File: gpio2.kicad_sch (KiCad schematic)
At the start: 2 parts, among them U27 RK3576

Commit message: Add files via upload
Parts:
- renumbered C329 to C99, U27 to U2
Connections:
- net PCIe_CLKREQ: no longer U2.1A17 (VI_CIF_D11)
- net PCIe_RESET: no longer U2.1A18 (VI_CIF_D12)
- net TYPEC_PWR-IN_SEL1: now reaches U2.1C18 (VI_CIF_D8)
- net TYPEC_PWR-IN_SEL2: now reaches U2.A21 (VI_CIF_D7)
- new net PCIE0_CLKREQn_M0: U2.1A17 (VI_CIF_D11)
- new net PCIE0_RESETn: U2.1A18 (VI_CIF_D12)
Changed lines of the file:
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@@
 		)
 	)
-	(label "PCIe_RESET"
+	(label "PCIE0_RESETn"
 		(at 147.32 53.34 180)
 		(effects
@@
 		)
 	)
+	(label "TYPEC_PWR-IN_SEL1"
+		(at 160.02 63.5 180)
+		(effects
+			(font
+				(size 1.016 1.016)
+			)
+			(justify right bottom)
+		)
+	)
 	(label "PCIe_WAKE"
 		(at 162.56 38.1 0)
@@
 		)
 	)
-	(label "PCIe_CLKREQ"
+	(label "PCIE0_CLKREQn_M0"
 		(at 147.32 55.88 180)
+		(effects
+			(font
+				(size 1.016 1.016)
+			)
+			(justify right bottom)
+		)
+	)
+	(label "TYPEC_PWR-IN_SEL2"
+		(at 160.02 66.04 180)
 		(effects
 			(font
@@
 		)
 	)
-	(hierarchical_label "PCIe_CTRL"
+	(hierarchical_label "PCIE0_CTRL"
 		(shape bidirectional)
 		(at 184.15 31.75 0)
+		(fields_autoplaced yes)
 		(effects
 			(font
@@
 			)
 			(justify left)
+		)
+		(property "Netclass" "PCIE0_CTRL"
+			(at 184.15 33.02 0)
+			(hide yes)
+			(show_name no)
+			(do_not_autoplace no)
+			(effects
+				(font
+					(size 1.27 1.27)
+					(italic yes)
+				)
+				(justify left)
+			)
 		)
 	)
@@
 			)
 			(justify left)
+		)
+	)
+	(rule_area
+		(exclude_from_sim no)
+		(in_bom yes)
+		(on_board yes)
+		(dnp no)
+		(polyline
+			(pts
+				(xy 129.54 67.31) (xy 130.81 66.04) (xy 147.32 66.04) (xy 148.59 67.31) (xy 148.59 82.55) (xy 147.32 83.82)
+				(xy 130.81 83.82) (xy 129.54 82.55)
+			)
+			(stroke
+				(width 0)
+				(type dash)
+			)
+			(fill
+				(type none)
+			)
 		)
 	)
@@
 		(in_pos_files yes)
 		(dnp no)
-		(property "Reference" "U27"
-			(at 101.092 27.94 0)
+		(property "Reference" "U2"
+			(at 101.092 35.306 0)
 			(show_name no)
 			(do_not_autoplace no)
@@
 		)
 		(property "Value" "RK3576"
-			(at 101.092 30.48 0)
+			(at 101.092 37.846 0)
 			(show_name no)
 			(do_not_autoplace no)
@@
 		(property "Manf" "Rockchip"
 			(at 101.092 33.02 0)
+			(hide yes)
 			(show_name no)
 			(do_not_autoplace no)
@@
 		(property "MPN" "RK3576"
 			(at 101.092 35.56 0)
+			(hide yes)
 			(show_name no)
 			(do_not_autoplace no)
@@
 		(property "Package" "FCCSP698L"
 			(at 101.092 38.1 0)
+			(hide yes)
+			(show_name no)
+			(do_not_autoplace no)
+			(effects
+				(font
+					(size 1.27 1.27)
+				)
+			)
+		)
+		(property "Dielectric" ""
+			(at 101.6 68.58 0)
+			(hide yes)
+			(show_name no)
+			(do_not_autoplace no)
+			(effects
+				(font
+					(size 1.27 1.27)
+				)
+			)
+		)
+		(property "Voltage" ""
+			(at 101.6 68.58 0)
+			(hide yes)
+			(show_name no)
+			(do_not_autoplace no)
+			(effects
+				(font
+					(size 1.27 1.27)
+				)
+			)
+		)
+		(property "KLC_S3.3" ""
+			(at 101.6 68.58 0)
+			(hide yes)
+			(show_name no)
+			(do_not_autoplace no)
+			(effects
+				(font
+					(size 1.27 1.27)
+				)
+			)
+		)
+		(property "KLC_S4.1" ""
+			(at 101.6 68.58 0)
+			(hide yes)
+			(show_name no)
+			(do_not_autoplace no)
+			(effects
+				(font
+					(size 1.27 1.27)
+				)
+			)
+		)
+		(property "KLC_S5.1" ""
+			(at 101.6 68.58 0)
+			(hide yes)
 			(show_name no)
 			(do_not_autoplace no)
@@
 			(project "RK3576 SBC"
 				(path "/b79dbff4-0cad-4ff7-bec2-7c0e4f8b14d3/34f9b0cb-aeae-42b4-a2af-a0a79afcf392/90f1d3d6-11a1-4fbf-aa1e-f6ffe7a54522"
-					(reference "U27")
+					(reference "U2")
 					(unit 3)
 				)
@@
 		(in_pos_files yes)
 		(dnp no)
-		(property "Reference" "#PWR0425"
+		(property "Reference" "#PWR0136"
 			(at 60.96 48.26 0)
 			(hide yes)
@@
 			(project "RK3576 SBC"
 				(path "/b79dbff4-0cad-4ff7-bec2-7c0e4f8b14d3/34f9b0cb-aeae-42b4-a2af-a0a79afcf392/90f1d3d6-11a1-4fbf-aa1e-f6ffe7a54522"
-					(reference "#PWR0425")
+					(reference "#PWR0136")
 					(unit 1)
 				)
@@
 		(dnp no)
 		(fields_autoplaced yes)
-		(property "Reference" "C329"
+		(property "Reference" "C99"
 			(at 63.5 45.7262 0)
 			(show_name no)
@@
 		)
 		(property "Description" "Unpolarized capacitor, small symbol"
+			(at 60.96 46.99 0)
+			(hide yes)
+			(show_name no)
+			(do_not_autoplace no)
+			(effects
+				(font
+					(size 1.27 1.27)
+				)
+			)
+		)
+		(property "Dielectric" ""
+			(at 60.96 46.99 0)
+			(hide yes)
+			(show_name no)
+			(do_not_autoplace no)
+			(effects
+				(font
+					(size 1.27 1.27)
+				)
+			)
+		)
+		(property "Voltage" ""
+			(at 60.96 46.99 0)
+			(hide yes)
+			(show_name no)
+			(do_not_autoplace no)
+			(effects
+				(font
+					(size 1.27 1.27)
+				)
+			)
+		)
+		(property "KLC_S3.3" ""
+			(at 60.96 46.99 0)
+			(hide yes)
+			(show_name no)
+			(do_not_autoplace no)
+			(effects
+				(font
+					(size 1.27 1.27)
+				)
+			)
+		)
+		(property "KLC_S4.1" ""
+			(at 60.96 46.99 0)
+			(hide yes)
+			(show_name no)
+			(do_not_autoplace no)
+			(effects
+				(font
+					(size 1.27 1.27)
+				)
+			)
+		)
+		(property "KLC_S5.1" ""
 			(at 60.96 46.99 0)
 			(hide yes)
@@
 			(project "RK3576 SBC"
 				(path "/b79dbff4-0cad-4ff7-bec2-7c0e4f8b14d3/34f9b0cb-aeae-42b4-a2af-a0a79afcf392/90f1d3d6-11a1-4fbf-aa1e-f6ffe7a54522"
-					(reference "C329")
+					(reference "C99")
 					(unit 1)
 				)
@@
 		(in_pos_files yes)
 		(dnp no)
-		(property "Reference" "#PWR0426"
+		(property "Reference" "#PWR0137"
 			(at 60.96 55.88 0)
 			(hide yes)
@@
 			(project "RK3576 SBC"
 				(path "/b79dbff4-0cad-4ff7-bec2-7c0e4f8b14d3/34f9b0cb-aeae-42b4-a2af-a0a79afcf392/90f1d3d6-11a1-4fbf-aa1e-f6ffe7a54522"
-					(reference "#PWR0426")
+					(reference "#PWR0137")
 					(unit 1)
 				)

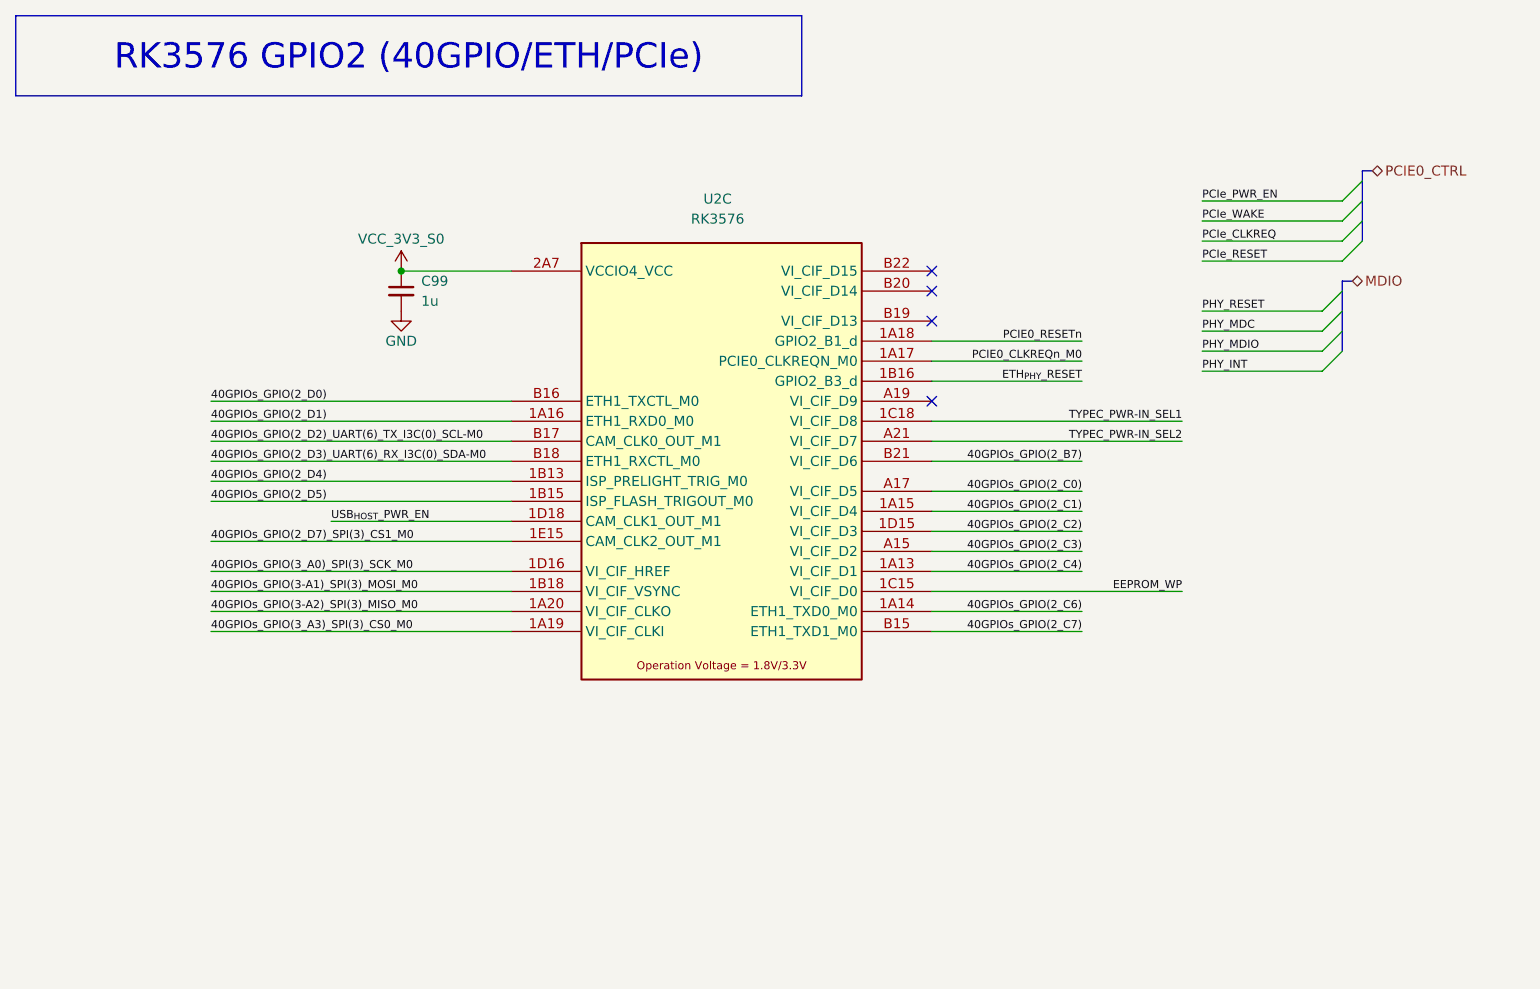
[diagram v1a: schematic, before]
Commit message: SBC Board V0.2
The SBC schematics before footprint and part number check
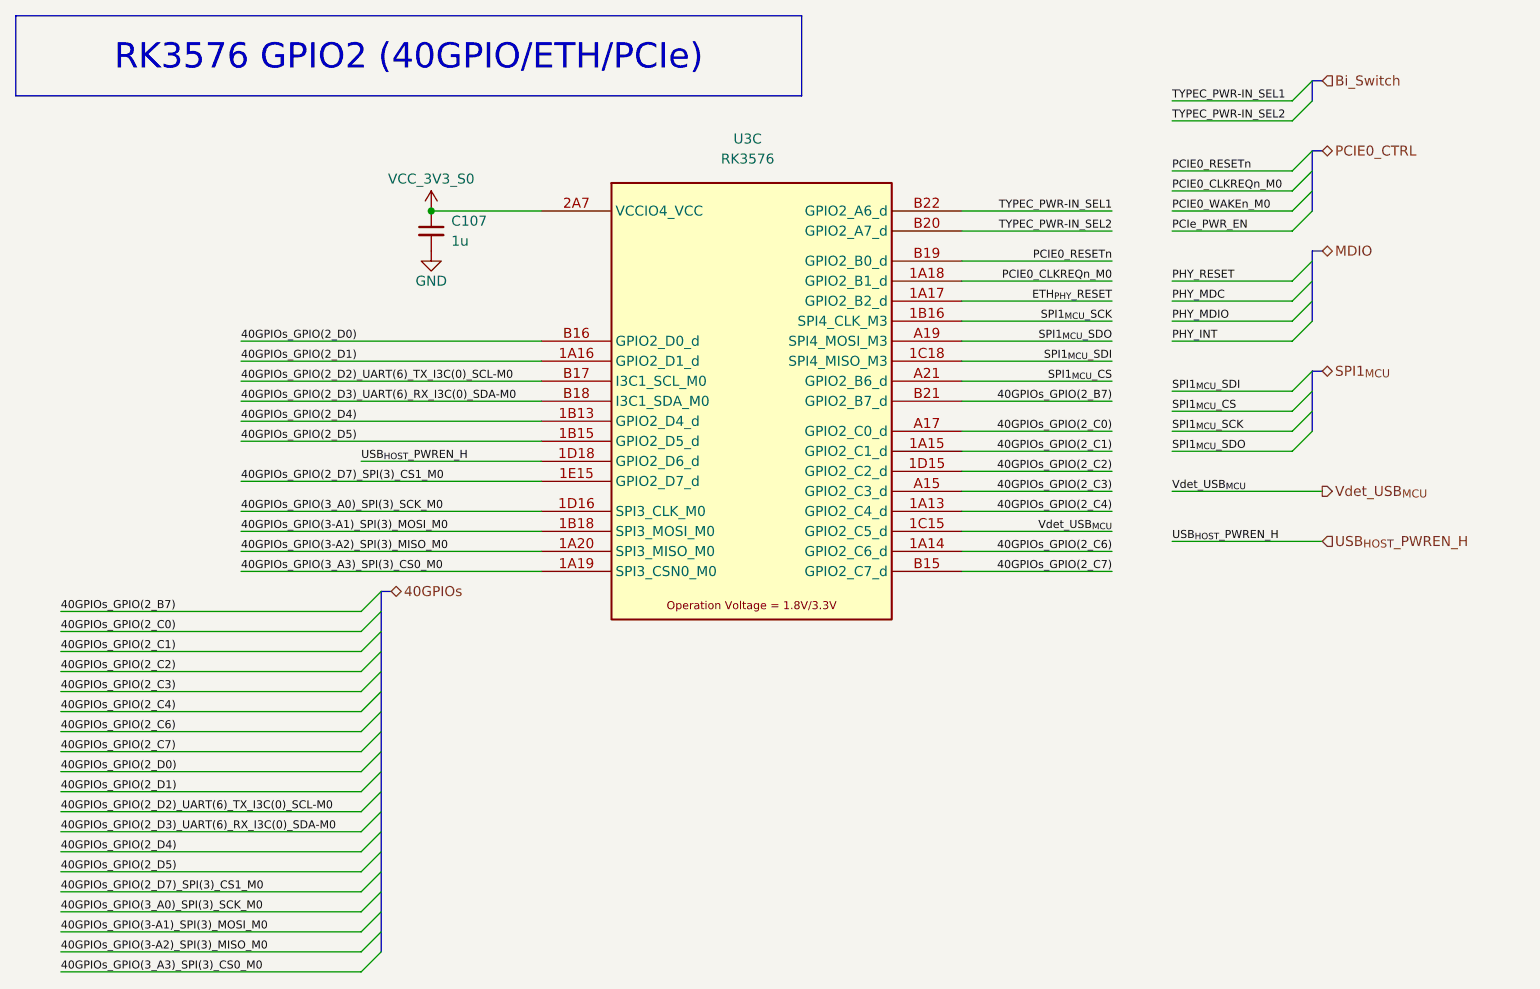
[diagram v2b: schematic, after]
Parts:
- U3: renamed from U2; footprint (none) -> easyeda2kicad:FCCSP-698_L17.2-W16.1-TL_RK3576
- renumbered C99 to C107
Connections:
- net ETH_{PHY}_RESET: now also U3.1A17 (VI_CIF_D11); no longer U3.1B16 (VI_CIF_D10)
- net PCIE0_CLKREQn_M0: now also U3.1A18 (VI_CIF_D12); no longer U3.1A17 (VI_CIF_D11)
- net PCIE0_RESETn: now also U3.B19 (VI_CIF_D13); no longer U3.1A18 (VI_CIF_D12)
- net TYPEC_PWR-IN_SEL1: now also U3.B22 (VI_CIF_D15); no longer U3.1C18 (VI_CIF_D8)
- net TYPEC_PWR-IN_SEL2: now also U3.B20 (VI_CIF_D14); no longer U3.A21 (VI_CIF_D7)
- net SPI1_{MCU}_SDO: now reaches U3.A19 (VI_CIF_D9)
- net EEPROM_WP renamed Vdet_USB_{MCU}
- net USB_{HOST}_PWR_EN renamed USB_{HOST}_PWREN_H
- new net SPI1_{MCU}_CS: U3.A21 (VI_CIF_D7)
- new net SPI1_{MCU}_SCK: U3.1B16 (VI_CIF_D10)
- new net SPI1_{MCU}_SDI: U3.1C18 (VI_CIF_D8)
- no-connect marks 4 -> 0
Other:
- moved on the sheet: C107, U3C

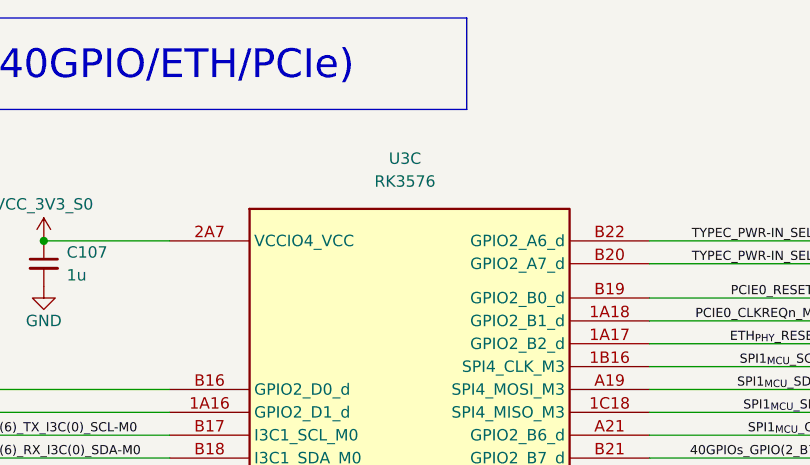
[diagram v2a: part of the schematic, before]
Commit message: SBCv0.3
there is no big thing update just some LCSC & Mouser parts
and Big problem deleted alot of component values (:
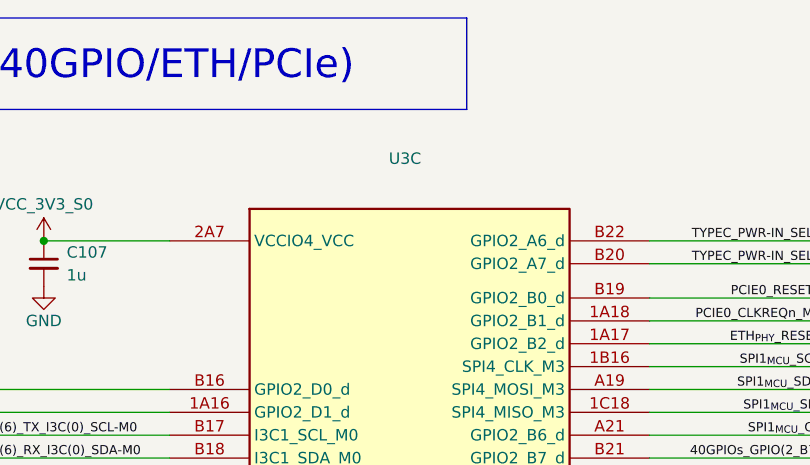
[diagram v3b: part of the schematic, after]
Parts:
- C107: footprint Capacitor_SMD:C_0402_1005Metric_Pad0.74x0.62mm_HandSolder -> Capacitor_SMD:C_0201_0603Metric_Pad0.64x0.40mm_HandSolder; LCSC Part (none) -> C5209398; Mouser Part (none) -> CL03A105KP3NSNC
- U3: value RK3576 -> (none); LCSC Part (none) -> (polyline
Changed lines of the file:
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@@
 			)
 		)
-		(property "Value" "RK3576"
+		(property "Value" ""
 			(at 104.902 30.226 0)
 			(show_name no)
@@
 			)
 		)
-		(property "KLC_S5.1" ""
+		(property "LCSC Part" "(polyline"
+			(at 105.41 60.96 0)
+			(hide yes)
+			(show_name no)
+			(do_not_autoplace no)
+			(effects
+				(font
+					(size 1.27 1.27)
+				)
+			)
+		)
+		(property "KLC_S4.2_DVDD" ""
+			(at 105.41 60.96 0)
+			(hide yes)
+			(show_name no)
+			(do_not_autoplace no)
+			(effects
+				(font
+					(size 1.27 1.27)
+				)
+			)
+		)
+		(property "KLC_S4.2_VREG_LX" ""
 			(at 105.41 60.96 0)
 			(hide yes)
@@
 					(reference "U3")
 					(unit 3)
+					(variant
+						(name "Test")
+					)
 				)
 			)
@@
 			)
 		)
-		(property "Footprint" "Capacitor_SMD:C_0402_1005Metric_Pad0.74x0.62mm_HandSolder"
+		(property "Footprint" "Capacitor_SMD:C_0201_0603Metric_Pad0.64x0.40mm_HandSolder"
 			(at 64.77 39.37 0)
 			(hide yes)
@@
 			)
 		)
-		(property "KLC_S5.1" ""
+		(property "LCSC Part" "C5209398"
+			(at 64.77 39.37 0)
+			(hide yes)
+			(show_name no)
+			(do_not_autoplace no)
+			(effects
+				(font
+					(size 1.27 1.27)
+				)
+			)
+		)
+		(property "Mouser Part" "CL03A105KP3NSNC "
+			(at 64.77 39.37 0)
+			(hide yes)
+			(show_name no)
+			(do_not_autoplace no)
+			(effects
+				(font
+					(size 1.27 1.27)
+				)
+			)
+		)
+		(property "KLC_S4.2_DVDD" ""
+			(at 64.77 39.37 0)
+			(hide yes)
+			(show_name no)
+			(do_not_autoplace no)
+			(effects
+				(font
+					(size 1.27 1.27)
+				)
+			)
+		)
+		(property "KLC_S4.2_VREG_LX" ""
 			(at 64.77 39.37 0)
 			(hide yes)
@@
 					(reference "C107")
 					(unit 1)
-				)
-			)
+					(variant
+						(name "Test")
+					)
+				)
+			)

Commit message: SBCv0.4
add LCSC & Mouser parts 
and solve the deleted value in the past version
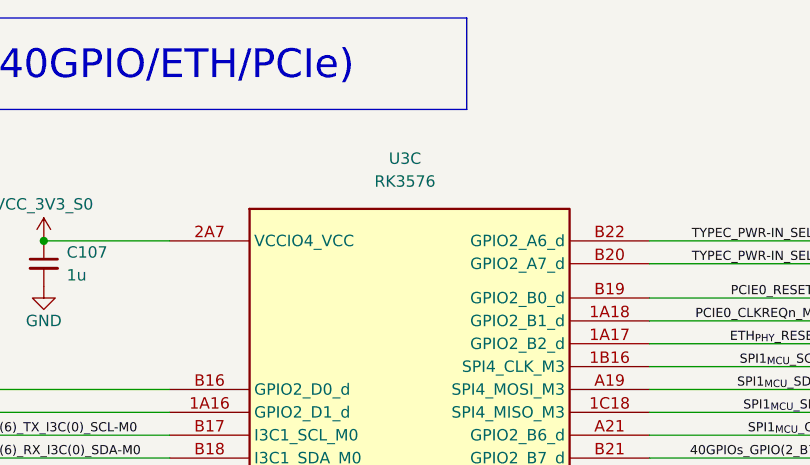
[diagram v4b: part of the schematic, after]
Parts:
- U3: value (none) -> RK3576; LCSC Part (polyline -> C42388007
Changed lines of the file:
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@@
 			)
 		)
-		(property "Value" ""
+		(property "Value" "RK3576"
 			(at 104.902 30.226 0)
 			(show_name no)
@@
 			)
 		)
-		(property "LCSC Part" "(polyline"
+		(property "LCSC Part" "C42388007"
 			(at 105.41 60.96 0)
 			(hide yes)
